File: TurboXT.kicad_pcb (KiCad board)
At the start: 2 copper layers, 25 parts, among them J1 8284 Socket, J2 HRQDMA, J3 DMAWAIT, J4 VCC, J5 GND, J6 Turbo LED, SW1 TURBO SWITCH, U1 8284, U2 74LS92, U3 74LS74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

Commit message: Gerbers + silkscreen
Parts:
- moved C2 96.8 mm to (59.1, 85.1), turned to 90 degrees
- moved C7 92.4 mm to (59.1, 67.9), turned to 270 degrees
- moved J3 81.0 mm to (72.4, 90.8)
- moved C8 79.6 mm to (58.4, 90.2)
- moved U3 73.8 mm to (62.9, 74.3), turned to 90 degrees
- moved C4 69.4 mm to (82.5, 68.6), turned to 270 degrees
- moved C6 68.8 mm to (82.5, 80.0), turned to 270 degrees
- moved J2 68.1 mm to (78.7, 90.8)
- moved U4 62.2 mm to (62.9, 86.4), turned to 90 degrees
- moved SW1 48.6 mm to (116.2, 68.6), turned to 270 degrees
- moved J5 43.9 mm to (116.8, 84.5)
- moved R2 42.0 mm to (107.3, 68.6), turned to 270 degrees
- moved C3 37.8 mm to (111.1, 78.7), turned to 90 degrees
- moved R1 37.3 mm to (111.1, 92.1), turned to 90 degrees
- moved J4 36.8 mm to (116.8, 89.5)
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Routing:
- net GND: track 0.00 -> 225.4 mm
- net VCC: track 0.00 -> 182.6 mm
- net /PCLK: track 0.00 -> 65.7 mm
- net /OSC: track 0.00 -> 62.9 mm
- net /TURBO_OSC: track 0.00 -> 59.9 mm
- net Net-(U3-Pad9): track 0.00 -> 42.5 mm
- net Net-(U3-Pad12): track 0.00 -> 37.2 mm
- net /TURBO: track 0.00 -> 36.6 mm
- net Net-(U3-Pad2): track 0.00 -> 35.1 mm
- net Net-(U3-Pad5): track 0.00 -> 35.0 mm
- net Net-(U4-Pad13): track 0.00 -> 26.9 mm
- net Net-(R1-Pad2): track 0.00 -> 20.7 mm
- net Net-(C3-Pad1): track 0.00 -> 19.9 mm
- net /EFI: track 0.00 -> 19.1 mm
- net Net-(U5-Pad12): track 0.00 -> 17.7 mm
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- added copper zone on B.Cu, net GND
- added copper zone on F.Cu, net GND
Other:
- board outline added: 74.3 x 43.8 mm
- net class Default: trace_width 0.25 -> 0.3
- net class POWER added: clearance 0.25, trace_width 0.5, via_dia 0.8, via_drill 0.4
- board text added: "+"
- board text added: "10k"
- board text added: "10uF"
- board text added: "1k"
- board text added: "24Mhz"
- board text added: "74LS00"
- board text added: "74LS02"
- board text added: "74LS14"
- board text added: "74LS74"
- board text added: "74LS92"
- board text added: "DMAWAIT"
- board text added: "GND"
- board text added: "HRQDMA"
- board text added: "LED"
- board text added: "Turbo"
- board text added: "TurboXT Rev. 1"
- board text added: "VCC"

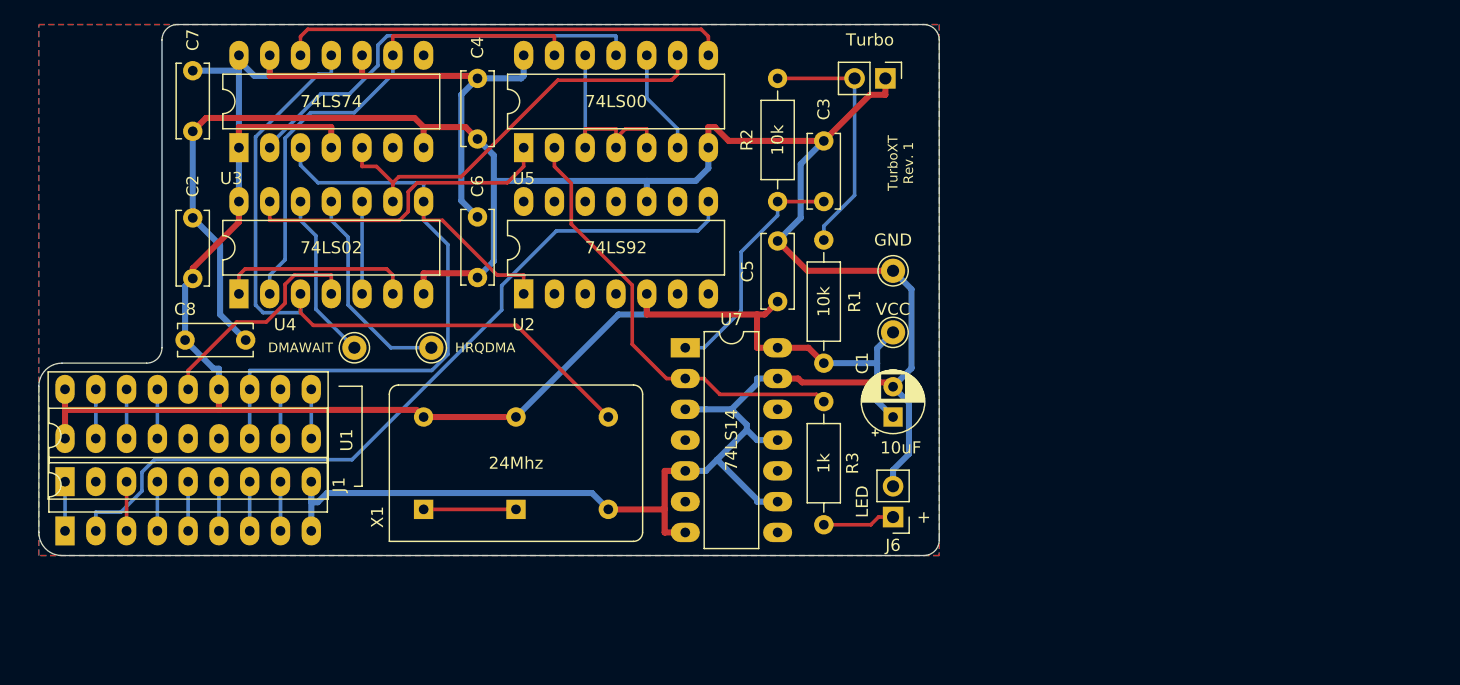
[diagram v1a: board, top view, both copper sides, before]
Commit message: Change connection for led
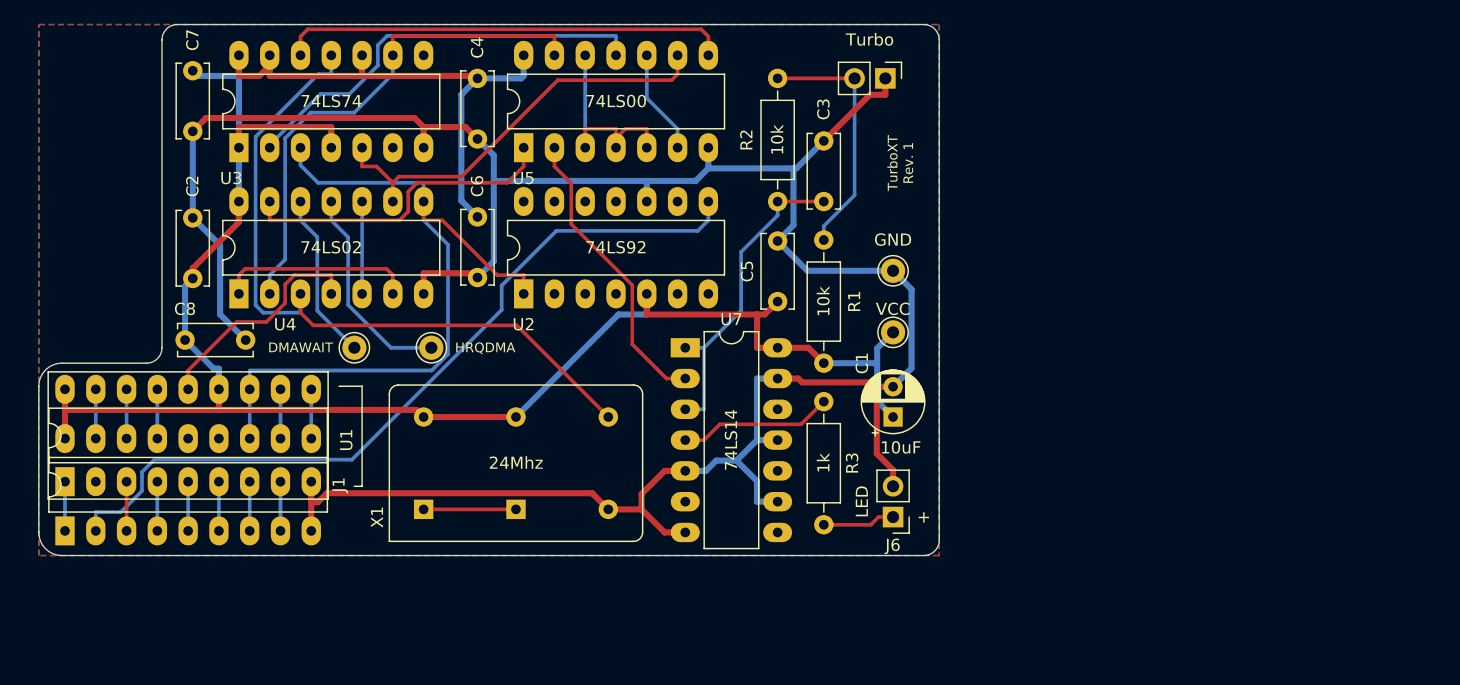
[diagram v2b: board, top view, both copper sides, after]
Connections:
- R3 pad 1: /TURBO -> Net-(R3-Pad1)
- U7 pad 3: GND -> Net-(C3-Pad1)
- U7 pad 4: Net-(U7-Pad4) -> Net-(R3-Pad1)
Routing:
- net Net-(R3-Pad1): track 0.00 -> 12.7 mm
- net /TURBO: track 36.6 -> 24.4 mm
- net GND: track 225.4 -> 214.2 mm
- net Net-(C3-Pad1): track 19.9 -> 26.6 mm

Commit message: Add notes to PCB and changed silkscreen
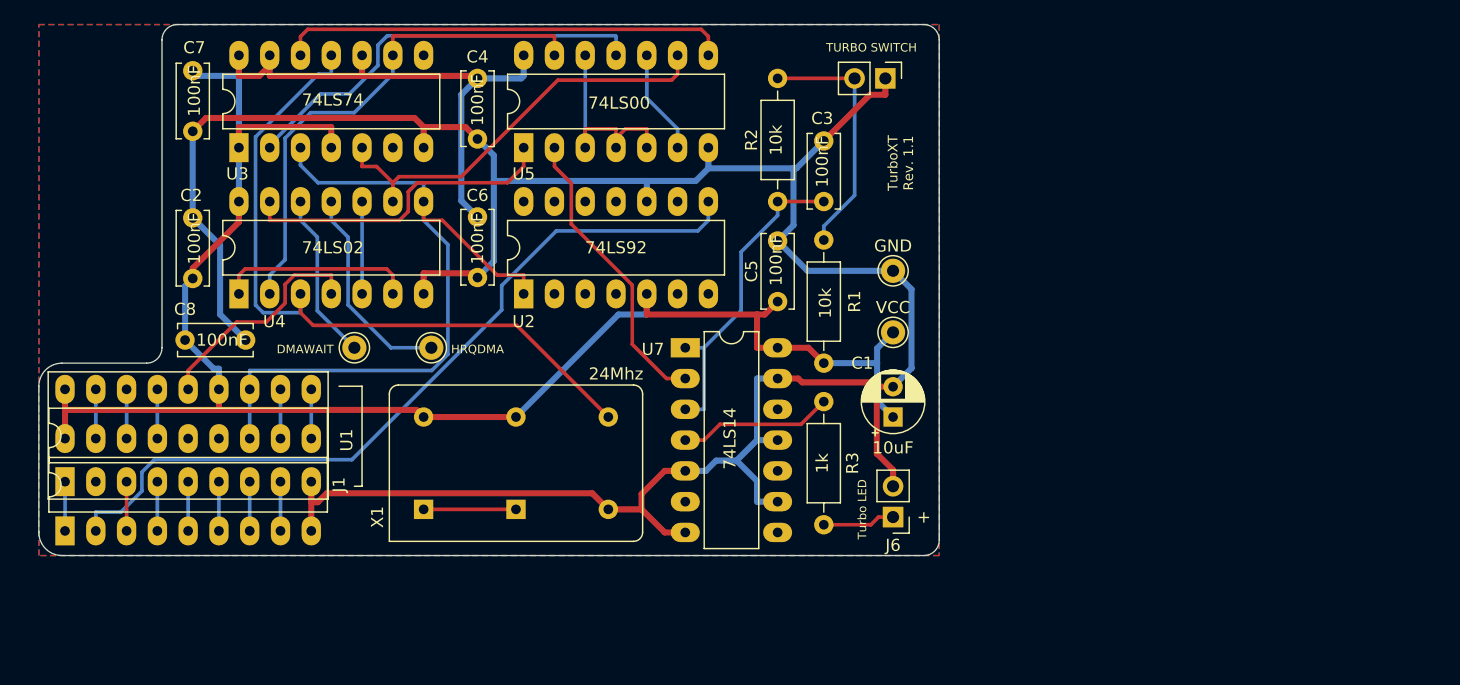
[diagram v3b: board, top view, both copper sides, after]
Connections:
- J1 pad 13: Net-(J1-Pad13) -> (no net)
- J1 pad 14: Net-(J1-Pad14) -> (no net)
- U1 pad 2: Net-(U1-Pad2) -> (no net)
- U2 pad 11: Net-(U2-Pad11) -> (no net)
- U2 pad 12: Net-(U2-Pad12) -> (no net)
- U2 pad 14: Net-(U2-Pad14) -> (no net)
- U2 pad 6: Net-(U2-Pad6) -> (no net)
- U2 pad 7: Net-(U2-Pad7) -> (no net)
- U2 pad 9: Net-(U2-Pad9) -> (no net)
- U3 pad 6: Net-(U3-Pad6) -> (no net)
- U3 pad 8: Net-(U3-Pad8) -> (no net)
- U7 pad 10: Net-(U7-Pad10) -> (no net)
- U7 pad 12: Net-(U7-Pad12) -> (no net)
- U7 pad 6: Net-(U7-Pad6) -> (no net)
- U7 pad 8: Net-(U7-Pad8) -> (no net)
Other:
- board text added: "TurboXT Rev. 1.1"
- board text removed: "10k"
- board text removed: "10uF"
- board text removed: "1k"
- board text removed: "24Mhz"
- board text removed: "74LS00"
- board text removed: "74LS02"
- board text removed: "74LS14"
- board text removed: "74LS74"
- board text removed: "74LS92"
- board text removed: "DMAWAIT"
- board text removed: "GND"
- board text removed: "HRQDMA"
- board text removed: "LED"
- board text removed: "Turbo"
- board text removed: "TurboXT Rev. 1"
- board text removed: "VCC"

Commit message: Connect reset of 74LS92
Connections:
- U2 pad 6: (no net) -> /RESET
- U2 pad 7: (no net) -> /RESET
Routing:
- net /RESET: track 4.06 -> 44.6 mm, vias 0 -> 1

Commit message: Change led value and silkscreen
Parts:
- R3: value 1k -> 470
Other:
- board text added: "TurboXT Rev. 1.2"
- board text removed: "TurboXT Rev. 1.1"

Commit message: Updated silkscreen
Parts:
- U7: value 74LS14 -> 74HCT14
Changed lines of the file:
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@@
       (effects (font (size 1 1) (thickness 0.15)))
     )
-    (fp_text value 74LS14 (at 3.683 7.493 270) (layer F.SilkS)
+    (fp_text value 74HCT14 (at 3.683 7.493 270) (layer F.SilkS)
       (effects (font (size 1 1) (thickness 0.15)))
     )

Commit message: Add reset button
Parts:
- added J7: Reset, Connector_PinHeader_2.54mm:PinHeader_1x02_P2.54mm_Vertical, F.Cu at (66.5, 90.7)
- added R4: 10k, Resistor_THT:R_Axial_DIN0207_L6.3mm_D2.5mm_P10.16mm_Horizontal, F.Cu at (72.1, 105.9)
- moved X1 1.52 mm to (79.6, 104.1)
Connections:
- J1 pad 11: /~RES -> Net-(J1-Pad11)
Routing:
- net VCC: track 182.6 -> 231.9 mm, vias 0 -> 1
- net Net-(J1-Pad11): track 0.00 -> 12.4 mm
- net /~RES: track 4.06 -> 11.0 mm
- net /PCLK: track 65.7 -> 71.8 mm
- net GND: track 214.2 -> 217.6 mm
- net /RESET: track 44.6 -> 47.7 mm
- net /TURBO_OSC: track 59.9 -> 62.8 mm
